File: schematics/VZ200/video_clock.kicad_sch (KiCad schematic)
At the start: 24 parts, among them J902 Monitor, Q1 1402B, Q1 1402D, U901 74LS390, U902 74LS393, U903 74LS21, U904 74LS00, U905 74LS86, U906 74LS390

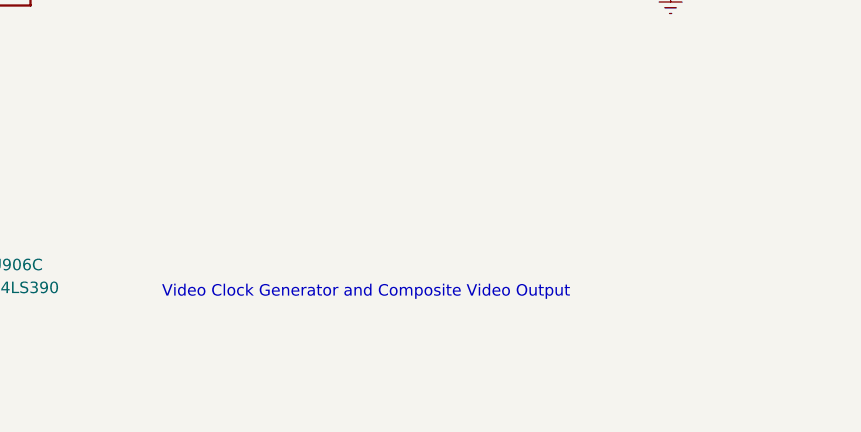
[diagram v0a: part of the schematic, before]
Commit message: Schematic for the VZ200 printer interface
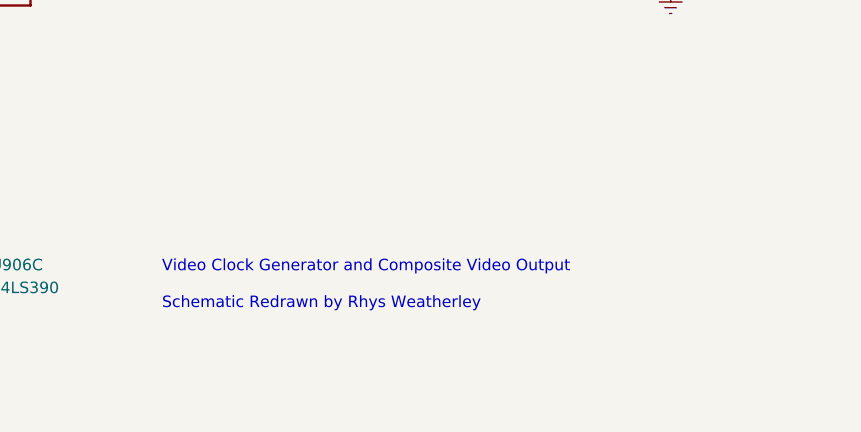
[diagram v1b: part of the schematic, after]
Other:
- note added: "Video Clock Generator and Composite Video Output Schematic Redrawn by Rhys Weatherley"
- note removed: "Video Clock Generator and Composite Video Output"
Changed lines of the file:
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@@
     (stroke (width 0) (type default))
   )
-  (text "Video Clock Generator and Composite Video Output" (at 180.34 175.895 0)
+  (text "Video Clock Generator and Composite Video Output\n\nSchematic Redrawn by Rhys Weatherley"
+    (at 180.34 177.165 0)
     (effects (font (size 1.27 1.27)) (justify left bottom))
   )

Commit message: Add title and revision details to the schematic sheets
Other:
- title: (none) -> VZ200 Computer
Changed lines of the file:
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@@
 (kicad_sch (version 20230121) (generator eeschema)
   (paper "A4")
+  (title_block
+    (title "VZ200 Computer")
+    (date "2024-01-01")
+    (rev "1")
+  )
   (junction (at 236.855 93.345) (diameter 0) (color 0 0 0 0)
   )

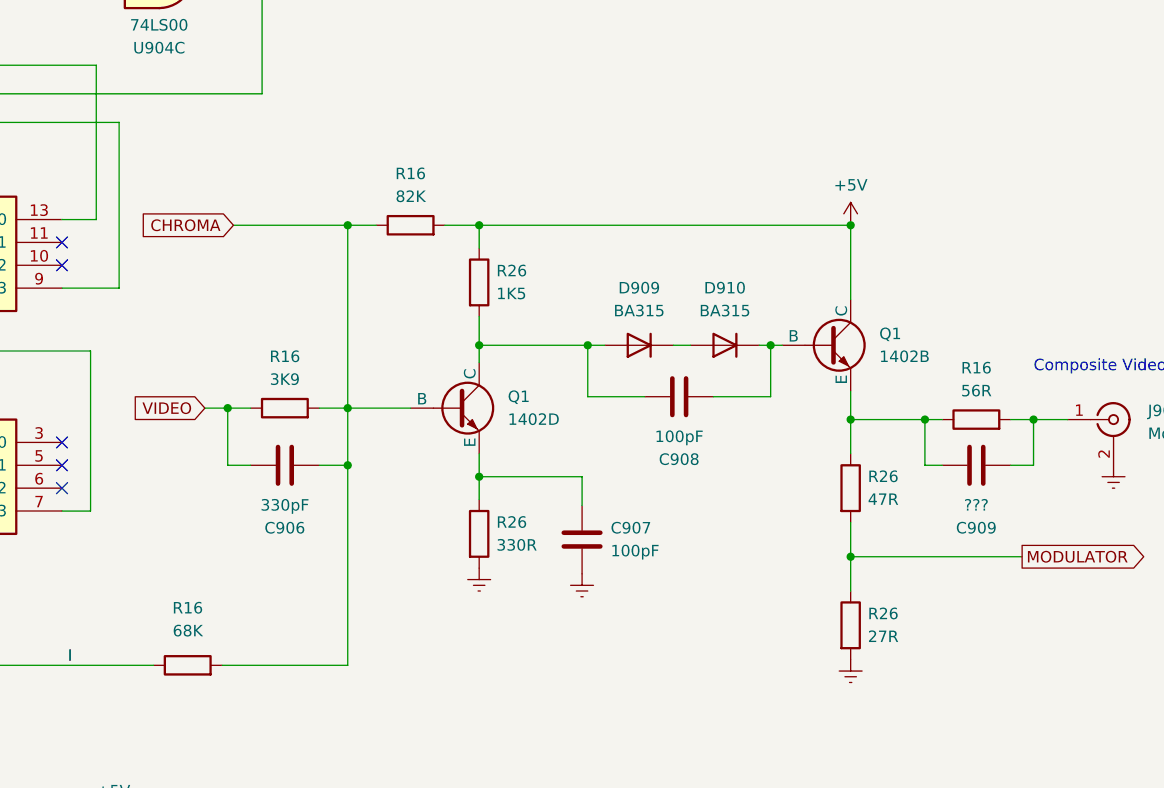
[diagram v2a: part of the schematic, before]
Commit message: Update motherboard schematic based on inspection of the actual board
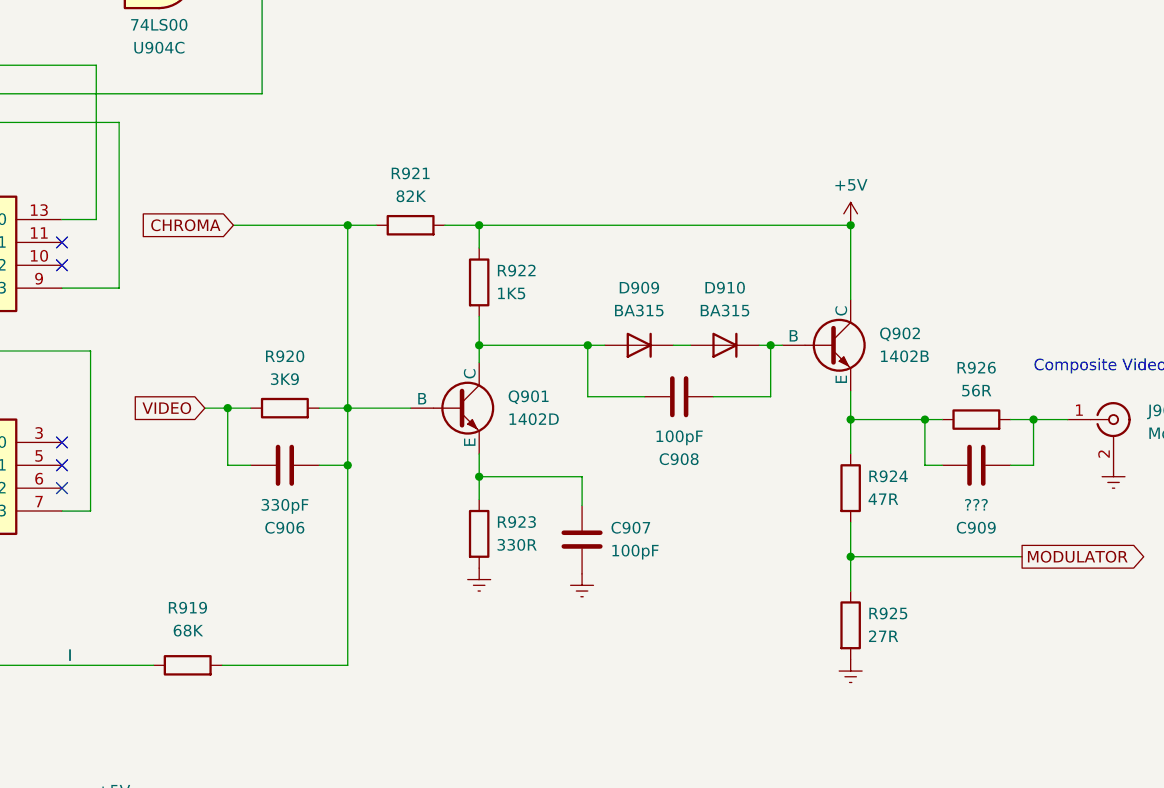
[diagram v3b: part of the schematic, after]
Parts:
- renumbered Q1 to Q901, Q1 to Q902, R16 to R919, R16 to R920, R16 to R921, R26 to R922, R26 to R923, R26 to R924, R26 to R925, R16 to R926
